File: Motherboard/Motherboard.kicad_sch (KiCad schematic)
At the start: 6 parts

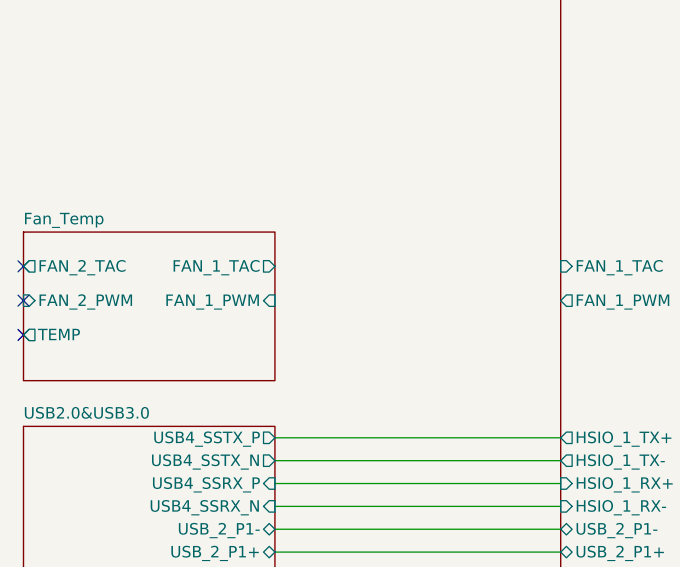
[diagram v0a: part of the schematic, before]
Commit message: Moved 3V3 and 5V converters to better fit the layout. Began Wiring for DDIB. Partially rewired TCP0 due to a schematic mistake.
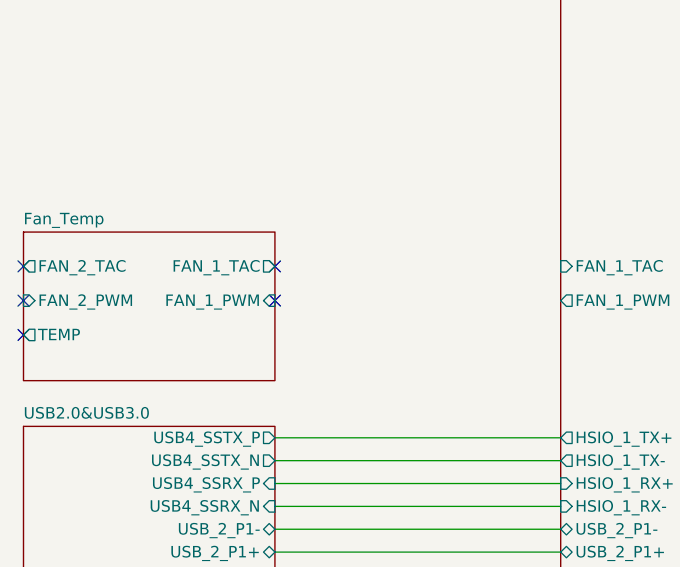
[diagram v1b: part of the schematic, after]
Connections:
- no-connect marks 3 -> 5
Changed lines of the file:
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@@
+	)
+	(no_connect
+		(at 208.28 278.13)
+	)
+	(no_connect
+		(at 208.28 274.32)
 	)
 	(no_connect

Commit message: Quick Save
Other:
- sheet EXIO ports: added RPi_HALL_L, RPi_HALL_R, SL_VOLT; removed none
- sheet LattePanda Module ports: added RPi_HALL_L, RPi_HALL_R; removed none
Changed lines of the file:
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@@
 	(wire
 		(pts
+			(xy 354.33 255.27) (xy 379.73 255.27)
+		)
+		(stroke
+			(width 0)
+			(type default)
+		)
+	)
+	(wire
+		(pts
 			(xy 354.33 71.12) (xy 379.73 71.12)
 		)
@@
 	(wire
 		(pts
+			(xy 354.33 257.81) (xy 379.73 257.81)
+		)
+		(stroke
+			(width 0)
+			(type default)
+		)
+	)
+	(wire
+		(pts
 			(xy 354.33 102.87) (xy 379.73 102.87)
 		)
@@
 	)
 	(symbol
+		(lib_id "power:+3V3")
+		(at 379.73 262.89 90)
+		(unit 1)
+		(body_style 1)
+		(exclude_from_sim no)
+		(in_bom yes)
+		(on_board yes)
+		(in_pos_files yes)
+		(dnp no)
+		(fields_autoplaced yes)
+		(property "Reference" "#PWR0177"
+			(at 383.54 262.89 0)
+			(hide yes)
+			(show_name no)
+			(do_not_autoplace no)
+			(effects
+				(font
+					(size 1.27 1.27)
+				)
+			)
+		)
+		(property "Value" "+3V3"
+			(at 375.92 262.8899 90)
+			(show_name no)
+			(do_not_autoplace no)
+			(effects
+				(font
+					(size 1.27 1.27)
+				)
+				(justify left)
+			)
+		)
+		(property "Footprint" ""
+			(at 379.73 262.89 0)
+			(hide yes)
+			(show_name no)
+			(do_not_autoplace no)
+			(effects
+				(font
+					(size 1.27 1.27)
+				)
+			)
+		)
+		(property "Datasheet" ""
+			(at 379.73 262.89 0)
+			(hide yes)
+			(show_name no)
+			(do_not_autoplace no)
+			(effects
+				(font
+					(size 1.27 1.27)
+				)
+			)
+		)
+		(property "Description" "Power symbol creates a global label with name \"+3V3\""
+			(at 379.73 262.89 0)
+			(hide yes)
+			(show_name no)
+			(do_not_autoplace no)
+			(effects
+				(font
+					(size 1.27 1.27)
+				)
+			)
+		)
+		(pin "1"
+		)
+		(instances
+			(project "Motherboard"
+				(path "/2a6d114a-7fd7-4207-b5f7-4ea9c34f36aa"
+					(reference "#PWR0177")
+					(unit 1)
+				)
+			)
+		)
+	)
+	(symbol
 		(lib_id "Mechanical:MountingHole_Pad")
 		(at 473.71 349.25 0)
@@
 			)
 		)
+		(pin "RPi_HALL_L" output
+			(at 354.33 255.27 0)
+			(effects
+				(font
+					(size 1.27 1.27)
+				)
+				(justify right)
+			)
+		)
+		(pin "RPi_HALL_R" output
+			(at 354.33 257.81 0)
+			(effects
+				(font
+					(size 1.27 1.27)
+				)
+				(justify right)
+			)
+		)
 		(instances
 			(project "Motherboard"
@@
 			)
 		)
+		(pin "RPi_HALL_L" output
+			(at 379.73 255.27 180)
+			(effects
+				(font
+					(size 1.27 1.27)
+				)
+				(justify left)
+			)
+		)
+		(pin "RPi_HALL_R" output
+			(at 379.73 257.81 180)
+			(effects
+				(font
+					(size 1.27 1.27)
+				)
+				(justify left)
+			)
+		)
+		(pin "SL_VOLT" input
+			(at 379.73 262.89 180)
+			(effects
+				(font
+					(size 1.27 1.27)
+				)
+				(justify left)
+			)
+		)

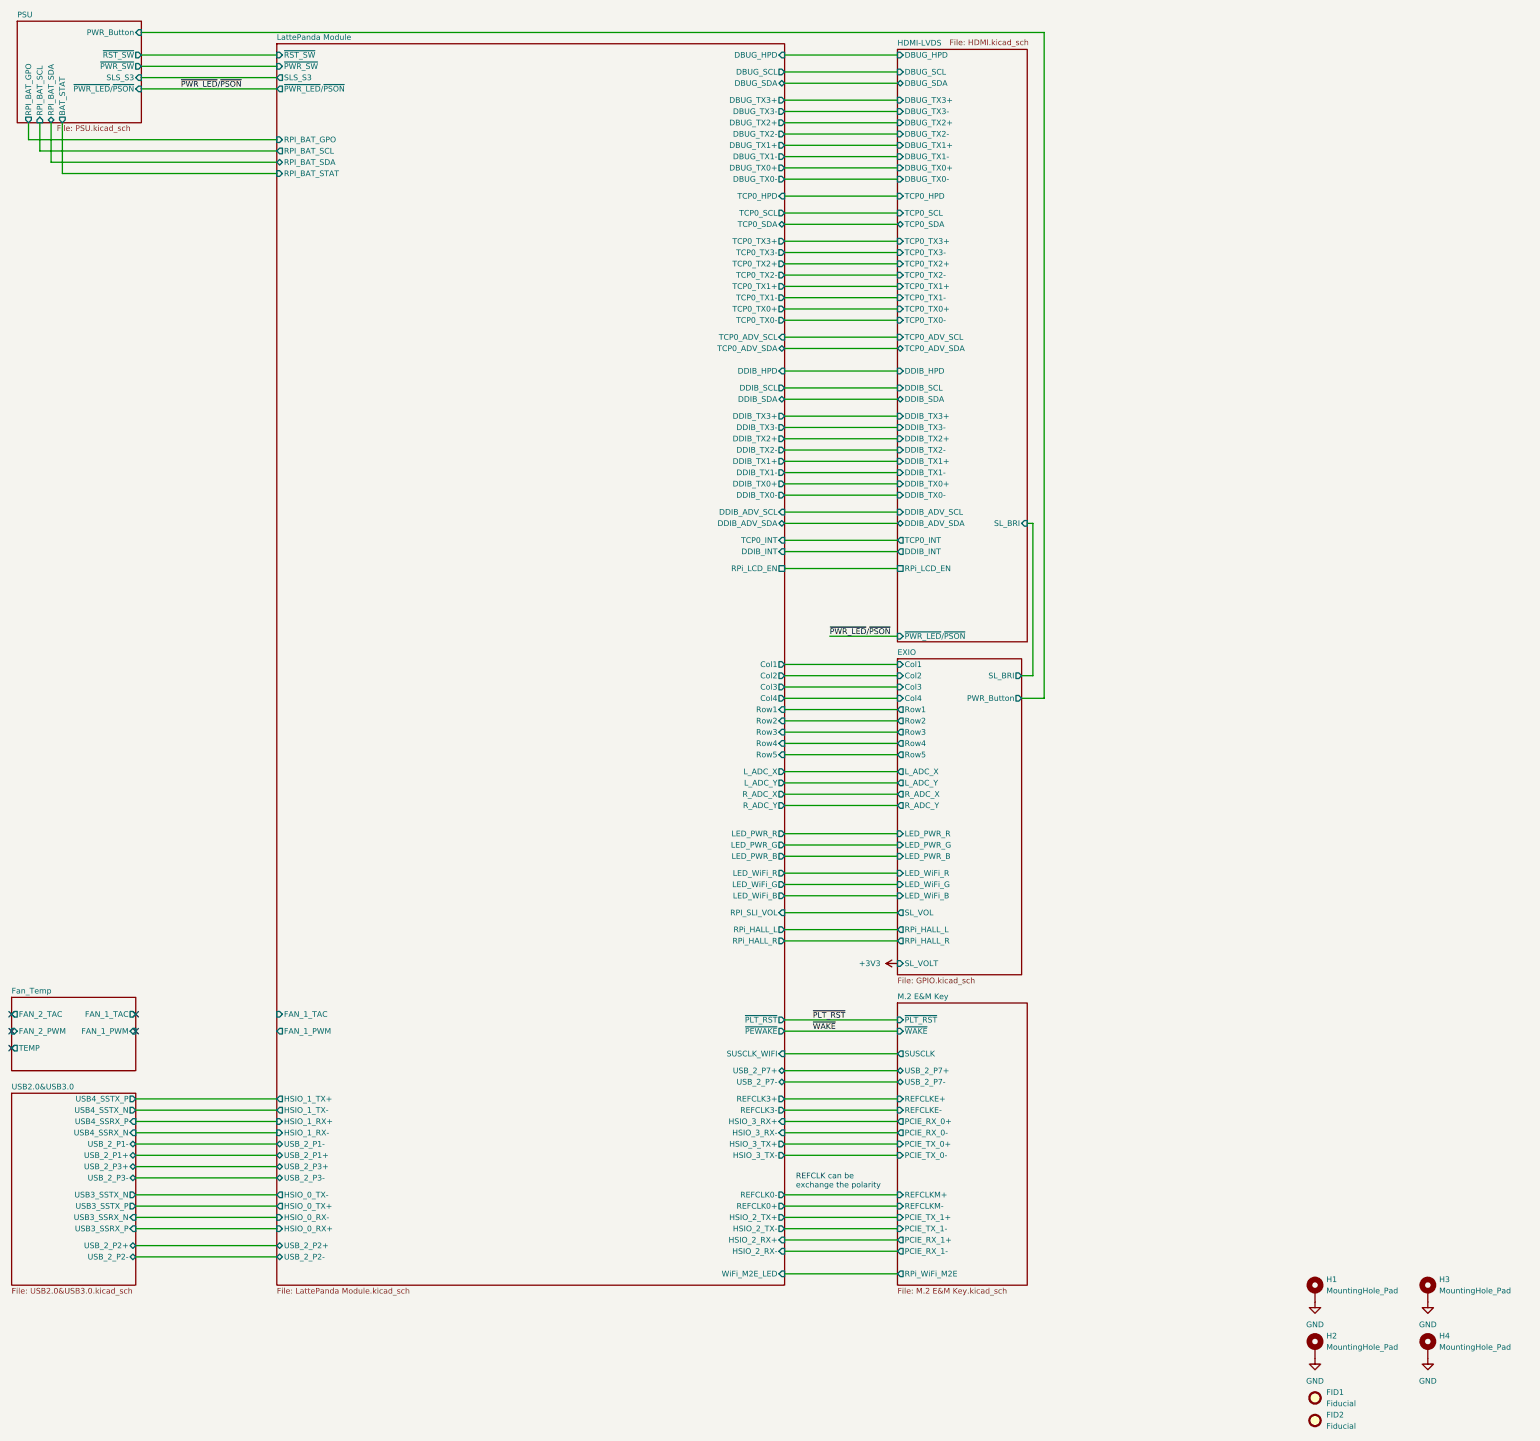
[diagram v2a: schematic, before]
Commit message: Removed CTRL_L_SLI as it is no longer used. Switched MCU from RP2040 to RP2354B, for the added ADC inputs.
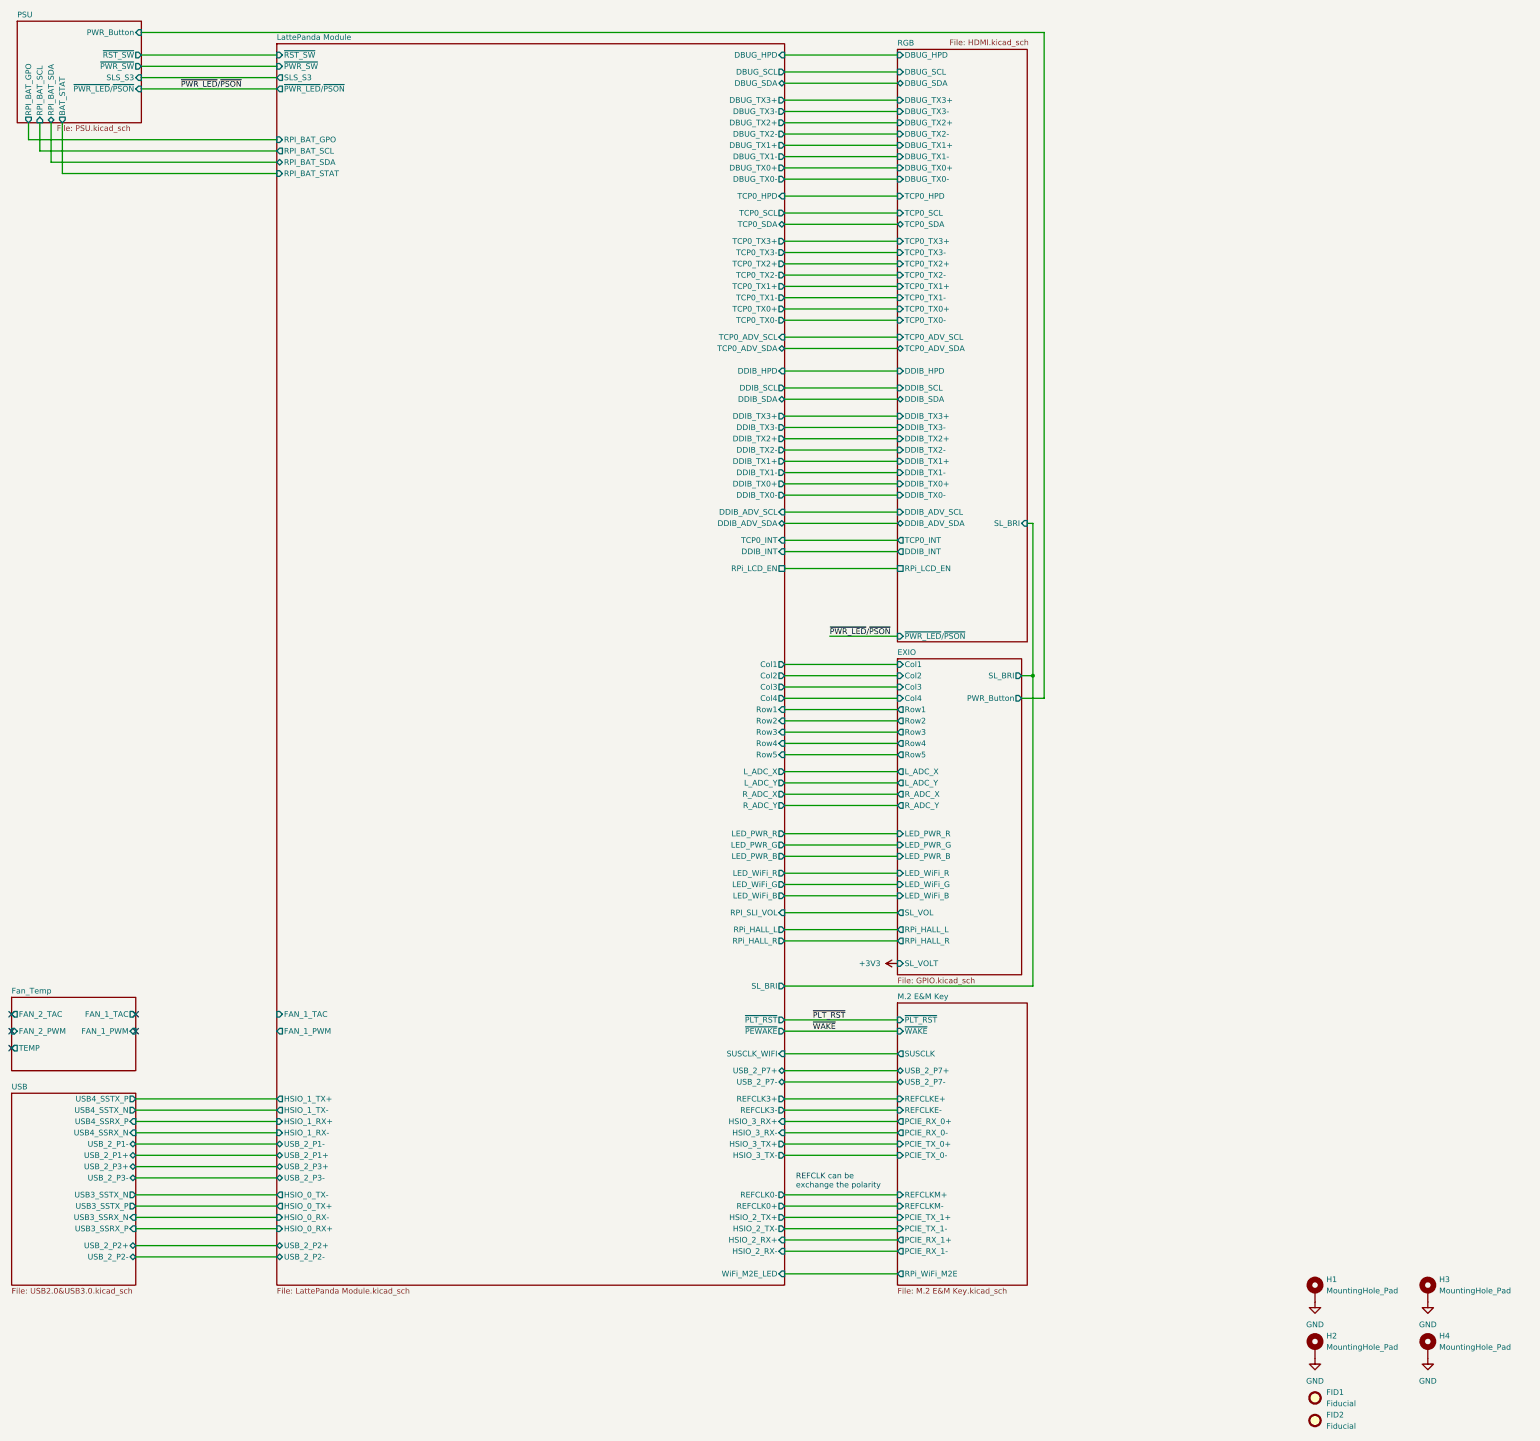
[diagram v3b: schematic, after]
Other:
- sheet HDMI-LVDS renamed RGB
- sheet USB2.0&USB3.0 renamed USB
- sheet LattePanda Module ports: added SL_BRI; removed none
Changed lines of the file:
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@@
 		)
 	)
+	(junction
+		(at 410.21 198.12)
+		(diameter 0)
+		(color 0 0 0 0)
+	)
 	(no_connect
 		(at 180.34 278.13)
@@
 	(wire
 		(pts
+			(xy 410.21 198.12) (xy 410.21 267.97)
+		)
+		(stroke
+			(width 0)
+			(type default)
+		)
+	)
+	(wire
+		(pts
 			(xy 354.33 68.58) (xy 379.73 68.58)
 		)
@@
 	(wire
 		(pts
+			(xy 354.33 267.97) (xy 410.21 267.97)
+		)
+		(stroke
+			(width 0)
+			(type default)
+		)
+	)
+	(wire
+		(pts
 			(xy 354.33 161.29) (xy 379.73 161.29)
 		)
@@
 			(color 0 0 0 0)
 		)
-		(property "Sheetname" "HDMI-LVDS"
+		(property "Sheetname" "RGB"
 			(at 379.73 56.4384 0)
 			(show_name no)
@@
 			)
 		)
+		(pin "SL_BRI" output
+			(at 354.33 267.97 0)
+			(effects
+				(font
+					(size 1.27 1.27)
+				)
+				(justify right)
+			)
+		)
 		(instances
 			(project "Motherboard"
@@
 			(color 0 0 0 0)
 		)
-		(property "Sheetname" "USB2.0&USB3.0"
+		(property "Sheetname" "USB"
 			(at 180.34 291.3884 0)
 			(show_name no)

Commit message: Many, Many fixes and changes. Mostly Schematic-related.
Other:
- sheet LattePanda Module ports: added DDIB_RST, DDIB_TOUCH_SCL, DDIB_TOUCH_SDA, RPi_5A_INT, RPi_5A_SCL, RPi_5A_SDA, TCP0_RST, TCP0_TOUCH_SCL, TCP0_TOUCH_SDA; removed none
- sheet PSU ports: added RPi_5A_INT, RPi_5A_SCL, RPi_5A_SDA; removed none
- sheet RGB ports: added DDIB_RST, DDIB_TOUCH_SCL, DDIB_TOUCH_SDA, TCP0_RST, TCP0_TOUCH_SCL, TCP0_TOUCH_SDA; removed none

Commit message: Various fixes, and some peripheral routing
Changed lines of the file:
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@@
-	)
-	(symbol
-		(lib_id "power:+3V3")
-		(at 379.73 262.89 90)
-		(unit 1)
-		(body_style 1)
-		(exclude_from_sim no)
-		(in_bom yes)
-		(on_board yes)
-		(in_pos_files yes)
-		(dnp no)
-		(fields_autoplaced yes)
-		(property "Reference" "#PWR0177"
-			(at 383.54 262.89 0)
-			(hide yes)
-			(show_name no)
-			(do_not_autoplace no)
-			(effects
-				(font
-					(size 1.27 1.27)
-				)
-			)
-		)
-		(property "Value" "+3V3"
-			(at 375.92 262.8899 90)
-			(show_name no)
-			(do_not_autoplace no)
-			(effects
-				(font
-					(size 1.27 1.27)
-				)
-				(justify left)
-			)
-		)
-		(property "Footprint" ""
-			(at 379.73 262.89 0)
-			(hide yes)
-			(show_name no)
-			(do_not_autoplace no)
-			(effects
-				(font
-					(size 1.27 1.27)
-				)
-			)
-		)
-		(property "Datasheet" ""
-			(at 379.73 262.89 0)
-			(hide yes)
-			(show_name no)
-			(do_not_autoplace no)
-			(effects
-				(font
-					(size 1.27 1.27)
-				)
-			)
-		)
-		(property "Description" "Power symbol creates a global label with name \"+3V3\""
-			(at 379.73 262.89 0)
-			(hide yes)
-			(show_name no)
-			(do_not_autoplace no)
-			(effects
-				(font
-					(size 1.27 1.27)
-				)
-			)
-		)
-		(pin "1"
-		)
-		(instances
-			(project "Motherboard"
-				(path "/2a6d114a-7fd7-4207-b5f7-4ea9c34f36aa"
-					(reference "#PWR0177")
-					(unit 1)
-				)
-			)
-		)
 	)
 	(symbol
